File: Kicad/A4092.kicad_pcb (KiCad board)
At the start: 4 copper layers, 175.6 x 122.1 mm, 106 parts, among them CN1 Zorro3, J1 Conn_02x25_Odd_Even, J2 Conn_01x06_Pin, J3 TO-LED, J4 TO-MB, J5 5787170-5, J7 22112042, J8 TO-A3000-LED, J9 TO-A3000-MB, SW1 219-8MST, U1 SN74ABT16543DGGR, U10 NCR53c710 SCSI Host Controller, U11 DS21S07A, U12 DS21S07A, U13 SST39SF010/020/040, U2 SN74ABT16543DGGR, U3 SN74ABT16543DGGR, U4 SN74ABT16543DGGR, U5 74LVC07APW_118, U6 SN74ABT16245ADGGR, U7 AMS1117-3.3, U8 SN74F244DB, U9 XC95144XL-TQ144, Y1 Abracon ACO-50MHz

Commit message: Your commit message
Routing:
- net Z_7M: track 2.64 -> 0.00 mm, vias 1 -> 0
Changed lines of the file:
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@@
-	)
-	(segment
-		(start 73.249999 77.749999)
-		(end 74.32565 77.749999)
-		(width 0.15)
-		(layer "F.Cu")
-		(net 80)
-	)
-	(segment
-		(start 72 77)
-		(end 72.5 77)
-		(width 0.15)
-		(layer "F.Cu")
-		(net 80)
-	)
-	(segment
-		(start 72.5 77)
-		(end 73.249999 77.749999)
-		(width 0.15)
-		(layer "F.Cu")
-		(net 80)
-	)
-	(via
-		(at 72 77)
-		(size 0.6)
-		(drill 0.3)
-		(layers "F.Cu" "B.Cu")
-		(net 80)
 	)
 	(segment

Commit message: Update PCB from schematics
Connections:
- CN1 pad 29: Z_A1 -> Z_LOCK
- U6 pad 26: PLD_DS1 -> PLD_DS0
- U9 pad 102: ROM_WE -> unconnected-(U9-P102-Pad102)
- U9 pad 107: ROM_OE -> unconnected-(U9-P107-Pad107)
- U9 pad 142: ROM_CE -> unconnected-(U9-P142-Pad142)
- U9 pad 2: PLD_FC0 -> unconnected-(U9-I/O/GTS3-Pad2)
- U9 pad 3: PLD_FC1 -> ROM_CE
- U9 pad 33: PLD_DS0 -> unconnected-(U9-P33-Pad33)
- U9 pad 34: PLD_DS1 -> unconnected-(U9-P34-Pad34)
- U9 pad 35: PLD_DS2 -> unconnected-(U9-P35-Pad35)
- U9 pad 39: PLD_DS3 -> unconnected-(U9-P39-Pad39)
- U9 pad 4: PLD_FC2 -> ROM_WE
- U9 pad 45: PLD_NACK -> unconnected-(U9-P45-Pad45)
- U9 pad 5: unconnected-(U9-I/O/GTS1-Pad5) -> ROM_OE
- U9 pad 75: unconnected-(U9-P75-Pad75) -> PLD_FC0
- U9 pad 76: unconnected-(U9-P76-Pad76) -> PLD_FC1
- U9 pad 77: unconnected-(U9-P77-Pad77) -> PLD_FC2
- U9 pad 78: unconnected-(U9-P78-Pad78) -> PLD_DS0
- U9 pad 79: unconnected-(U9-P79-Pad79) -> PLD_DS1
- U9 pad 80: unconnected-(U9-P80-Pad80) -> PLD_DS2
- U9 pad 81: unconnected-(U9-P81-Pad81) -> PLD_DS3
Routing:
- net unconnected-(U9-P142-Pad142): track 0.00 -> 14.1 mm
- net ROM_CE: track 14.1 -> 0.00 mm

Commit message: routin gin progress
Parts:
- moved C15 3.00 mm to (83.0, 99.5), turned to 0 degrees
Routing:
- net A18: track 57.7 -> 148.4 mm, vias 1 -> 3
- net A19: track 57.8 -> 139.7 mm, vias 1 -> 2
- net A17: track 28.9 -> 110.7 mm, vias 1 -> 3
- net PLD_FC0: track 2.80 -> 56.2 mm, vias 0 -> 1
- net PLD_FC1: track 1.88 -> 39.1 mm, vias 0 -> 1
- net ROM_WE: track 0.00 -> 27.7 mm, vias 0 -> 1
- net SREG: track 54.5 -> 76.6 mm, vias 1 -> 2
- net TDO: track 7.49 -> 27.1 mm, vias 0 -> 1
- net ROM_OE: track 0.00 -> 19.2 mm, vias 0 -> 2
- net CBREQ: track 56.5 -> 38.2 mm
- net ROM_CE: track 0.00 -> 18.1 mm
- net BERR: track 29.4 -> 47.3 mm
- net SLACK: track 59.2 -> 76.9 mm, vias 1 -> 2
- net CBACK: track 30.9 -> 48.3 mm, vias 1 -> 2
- net STERM: track 21.9 -> 36.9 mm, vias 1 -> 2
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
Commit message: Update from schematics
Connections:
- C30 pad 2: Net-(C30-Pad2) -> GND
- C31 pad 2: Net-(C30-Pad2) -> GND
- RN16 pad 2: Z_SENSE3 -> Z_SENSEZ3

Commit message: Routing in progress
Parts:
- moved C11 0.50 mm to (74.0, 99.5)
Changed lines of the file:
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@@
 	(footprint "Capacitor_SMD:C_0603_1608Metric_Pad1.08x0.95mm_HandSolder"
 		(layer "F.Cu")
-		(at 73.5 99.5 180)
+		(at 74 99.5 180)
 		(descr "Capacitor SMD 0603 (1608 Metric), square (rectangular) end terminal, IPC_7351 nominal with elongated pad for handsoldering. (Body size source: IPC-SM-782 page 76, https://www.pcb-3d.com/wordpress/wp-content/uploads/ipc-sm-782a_amendment_1_and_2.pdf), generated with kicad-footprint-generator")
 		(tags "capacitor handsolder")

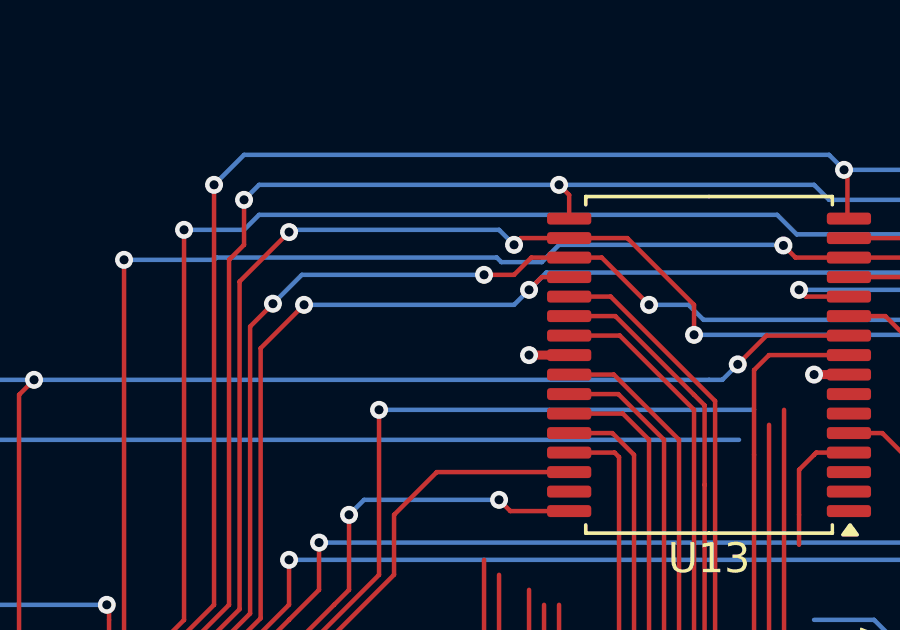
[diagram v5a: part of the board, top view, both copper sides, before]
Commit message: Add pulldown of ROM_CE to PCB
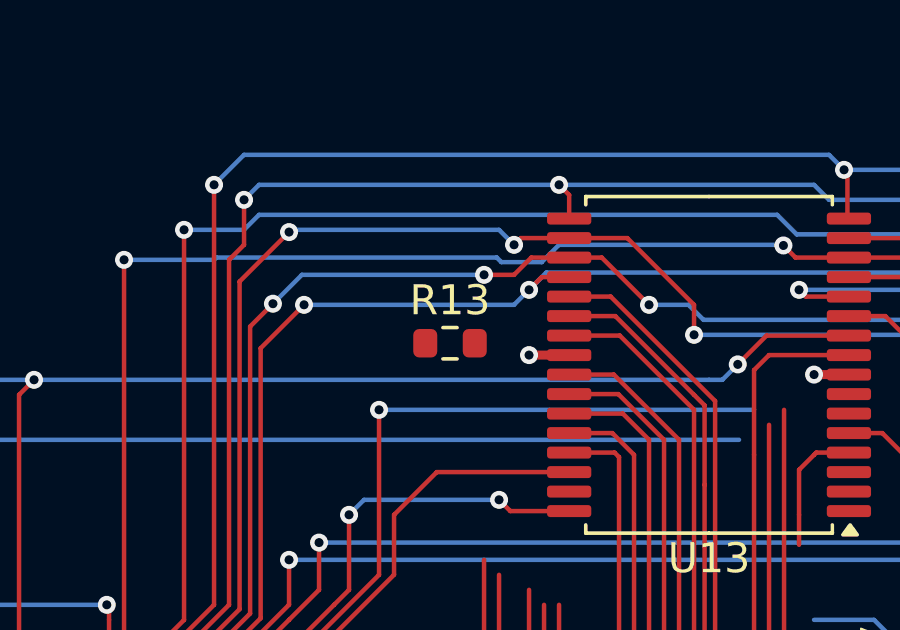
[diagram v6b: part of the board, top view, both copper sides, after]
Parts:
- added R13: 1K, Resistor_SMD:R_0603_1608Metric, F.Cu at (100.4, 60.3)
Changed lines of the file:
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@@
 		(fp_text user "*"
 			(at -11.9888 -9.381 270)
-			(unlocked yes)
 			(layer "F.SilkS")
 			(effects
@@
 		(fp_text user "*"
 			(at -11.9888 -9.381 270)
+			(unlocked yes)
 			(layer "F.SilkS")
 			(effects
@@
 			(offset
 				(xyz 0 0 0)
+			)
+			(scale
+				(xyz 1 1 1)
+			)
+			(rotate
+				(xyz 0 0 0)
+			)
+		)
+	)
+	(footprint "Resistor_SMD:R_0603_1608Metric"
+		(layer "F.Cu")
+		(at 100.365 60.28)
+		(descr "Resistor SMD 0603 (1608 Metric), square (rectangular) end terminal, IPC-7351 nominal, (Body size source: IPC-SM-782 page 72, https://www.pcb-3d.com/wordpress/wp-content/uploads/ipc-sm-782a_amendment_1_and_2.pdf), generated with kicad-footprint-generator")
+		(tags "resistor")
+		(property "Reference" "R13"
+			(at 0 -1.43 0)
+			(layer "F.SilkS")
+			(effects
+				(font
+					(size 1 1)
+					(thickness 0.15)
+				)
+			)
+		)
+		(property "Value" "1K"
+			(at 0 1.43 0)
+			(layer "F.Fab")
+			(effects
+				(font
+					(size 1 1)
+					(thickness 0.15)
+				)
+			)
+		)
+		(property "Datasheet" ""
+			(at 0 0 0)
+			(layer "F.Fab")
+			(hide yes)
+			(effects
+				(font
+					(size 1.27 1.27)
+					(thickness 0.15)
+				)
+			)
+		)
+		(property "Description" "Resistor, small symbol"
+			(at 0 0 0)
+			(layer "F.Fab")
+			(hide yes)
+			(effects
+				(font
+					(size 1.27 1.27)
+					(thickness 0.15)
+				)
+			)
+		)
+		(property ki_fp_filters "R_*")
+		(sheetname "/SCSI-2 Controller/")
+		(sheetfile "scsi2.kicad_sch")
+		(attr smd)
+		(fp_line
+			(start -0.237258 -0.5225)
+			(end 0.237258 -0.5225)
+			(stroke
+				(width 0.12)
+				(type solid)
+			)
+			(layer "F.SilkS")
+		)
+		(fp_line
+			(start -0.237258 0.5225)
+			(end 0.237258 0.5225)
+			(stroke
+				(width 0.12)
+				(type solid)
+			)
+			(layer "F.SilkS")
+		)
+		(fp_line
+			(start -1.48 -0.73)
+			(end 1.48 -0.73)
+			(stroke
+				(width 0.05)
+				(type solid)
+			)
+			(layer "F.CrtYd")
+		)
+		(fp_line
+			(start -1.48 0.73)
+			(end -1.48 -0.73)
+			(stroke
+				(width 0.05)
+				(type solid)
+			)
+			(layer "F.CrtYd")
+		)
+		(fp_line
+			(start 1.48 -0.73)
+			(end 1.48 0.73)
+			(stroke
+				(width 0.05)
+				(type solid)
+			)
+			(layer "F.CrtYd")
+		)
+		(fp_line
+			(start 1.48 0.73)
+			(end -1.48 0.73)
+			(stroke
+				(width 0.05)
+				(type solid)
+			)
+			(layer "F.CrtYd")
+		)
+		(fp_line
+			(start -0.8 -0.4125)
+			(end 0.8 -0.4125)
+			(stroke
+				(width 0.1)
+				(type solid)
+			)
+			(layer "F.Fab")
+		)
+		(fp_line
+			(start -0.8 0.4125)
+			(end -0.8 -0.4125)
+			(stroke
+				(width 0.1)
+				(type solid)
+			)
+			(layer "F.Fab")
+		)
+		(fp_line
+			(start 0.8 -0.4125)
+			(end 0.8 0.4125)
+			(stroke
+				(width 0.1)
+				(type solid)
+			)
+			(layer "F.Fab")
+		)
+		(fp_line
+			(start 0.8 0.4125)
+			(end -0.8 0.4125)
+			(stroke
+				(width 0.1)
+				(type solid)
+			)
+			(layer "F.Fab")
+		)
+		(fp_text user "${REFERENCE}"
+			(at 0 0 0)
+			(layer "F.Fab")
+			(effects
+				(font
+					(size 0.4 0.4)
+					(thickness 0.06)
+				)
+			)
+		)
+		(pad "1" smd roundrect
+			(at -0.825 0)
+			(size 0.8 0.95)
+			(layers "F.Cu" "F.Mask" "F.Paste")
+			(roundrect_rratio 0.25)
+			(net 363 "ROM_CE")
+			(pintype "passive")
+		)
+		(pad "2" smd roundrect
+			(at 0.825 0)
+			(size 0.8 0.95)
+			(layers "F.Cu" "F.Mask" "F.Paste")
+			(roundrect_rratio 0.25)
+			(net 1 "GND")
+			(pintype "passive")
+		)
+		(embedded_fonts no)
+		(model "${KICAD9_3DMODEL_DIR}/Resistor_SMD.3dshapes/R_0603_1608Metric.wrl"
+			(offset
+				(xyz 0 0 0)

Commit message: Routing
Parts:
- moved C28 85.6 mm to (174.5, 141.5), turned to 0 degrees
- moved C20 83.1 mm to (110.0, 142.5)
- moved C19 81.1 mm to (124.0, 141.0)
- moved C21 78.5 mm to (174.5, 125.5), turned to 0 degrees
- moved C22 76.7 mm to (162.5, 141.5), turned to 180 degrees
- moved C27 73.7 mm to (165.0, 126.0), turned to 0 degrees
- moved C29 73.1 mm to (108.5, 125.5)
- moved C18 55.0 mm to (122.5, 125.5), turned to 0 degrees
- moved C46 44.6 mm to (55.5, 124.5), turned to 180 degrees
- moved C26 40.8 mm to (138.0, 141.0), turned to 180 degrees
- moved C25 39.6 mm to (149.5, 141.0)
- moved C23 39.4 mm to (148.5, 125.5), turned to 0 degrees
- moved U7 32.8 mm to (55.5, 115.0), turned to 90 degrees
- moved C30 27.3 mm to (160.0, 108.5)
- moved C24 23.8 mm to (137.0, 126.0)
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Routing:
- net MASTER: track 25.0 -> 59.2 mm, vias 1 -> 2
- net CLK: track 12.8 -> 44.4 mm, vias 1 -> 2
- net SBR: track 73.5 -> 101.1 mm, vias 1 -> 2
- net V5: track 98.0 -> 73.4 mm, vias 15 -> 14
- net IORST: track 112.4 -> 136.7 mm, vias 2 -> 3
- net BMASTER: track 3.43 -> 26.1 mm
- net DBLT: track 4.14 -> 26.6 mm
- net DBOE: track 0.00 -> 19.6 mm
- net GND: track 155.7 -> 136.6 mm, vias 44 -> 43
- net Z2D: track 0.00 -> 18.6 mm
- net Z_INT2: track 4.93 -> 23.4 mm
- net PLD_FC2: track 1.31 -> 19.4 mm
- net ABOEL: track 6.14 -> 23.6 mm
- net PLD_DS0: track 0.00 -> 17.1 mm
- net D2Z: track 6.14 -> 23.1 mm
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
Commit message: Routing
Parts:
- moved J4 16.6 mm to (70.5, 46.0)
- moved J8 14.5 mm to (84.0, 36.5)
- moved J9 3.99 mm to (84.1, 46.0)
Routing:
- net LED: track 0.00 -> 120.0 mm, vias 0 -> 2
- net A19: track 146.1 -> 96.9 mm, vias 3 -> 4
- net A22: track 13.2 -> 61.0 mm, vias 1 -> 2
- net PLD_FC0: track 56.2 -> 10.6 mm, vias 1 -> 0
- net D4: track 87.7 -> 132.7 mm, vias 1 -> 3
- net A18: track 148.2 -> 107.1 mm, vias 3 -> 2
- net A21: track 20.7 -> 61.4 mm, vias 1 -> 2
- net D5: track 101.6 -> 140.1 mm, vias 1 -> 2
- net SCTRL_ACK: track 86.2 -> 121.6 mm, vias 4 -> 6
- net A16: track 25.1 -> 59.4 mm
- net A17: track 112.5 -> 146.1 mm, vias 4 -> 6
- net SCTRL_MSG: track 85.2 -> 116.2 mm, vias 4 -> 6
- net SCTRL_IO: track 93.8 -> 123.0 mm, vias 4 -> 6
- net A20: track 26.6 -> 55.2 mm
- net LEDR: track 0.00 -> 28.6 mm
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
